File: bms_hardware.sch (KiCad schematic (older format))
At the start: 0 parts

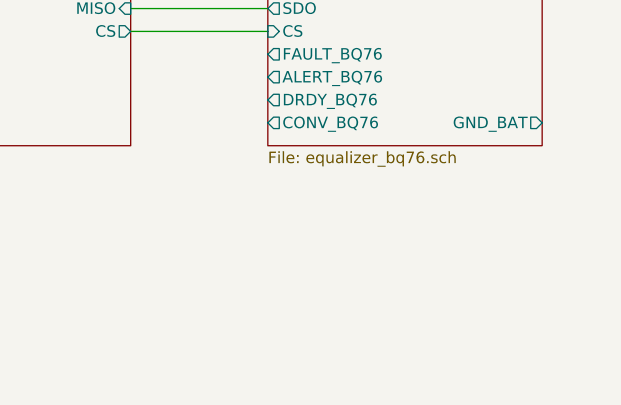
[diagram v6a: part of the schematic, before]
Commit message: Added bat_charger.sch to main hierarchical bms project
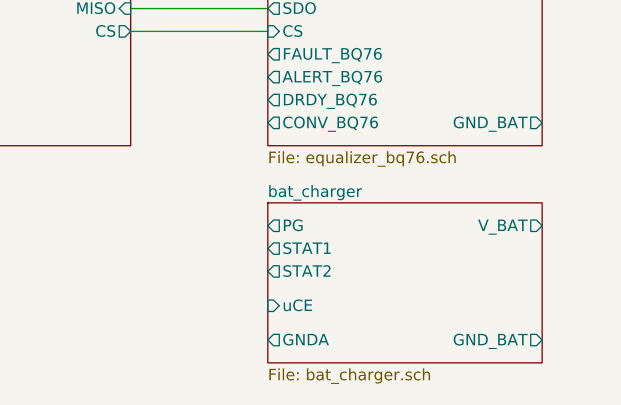
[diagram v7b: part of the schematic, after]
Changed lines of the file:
@@
 $Descr A4 11693 8268
 encoding utf-8
-Sheet 1 5
+Sheet 1 6
 Title ""
 Date ""
@@
 Wire Wire Line
 	6400 4100 7000 4100
+$Sheet
+S 7000 4850 1200 700
+U 60006E35
+F0 "bat_charger" 50
+F1 "bat_charger.sch" 50
+F2 "V_BAT" O R 8200 4950 50
+F3 "GND_BAT" O R 8200 5450 50
+F4 "STAT1" O L 7000 5050 50
+F5 "STAT2" O L 7000 5150 50
+F6 "PG" O L 7000 4950 50
+F7 "uCE" I L 7000 5300 50
+F8 "GNDA" O L 7000 5450 50
+$EndSheet
 $EndSCHEMATC
